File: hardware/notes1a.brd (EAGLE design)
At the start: 160 x 100 mm, 4 parts, among them U1 LMP7721, U2 MAX4477

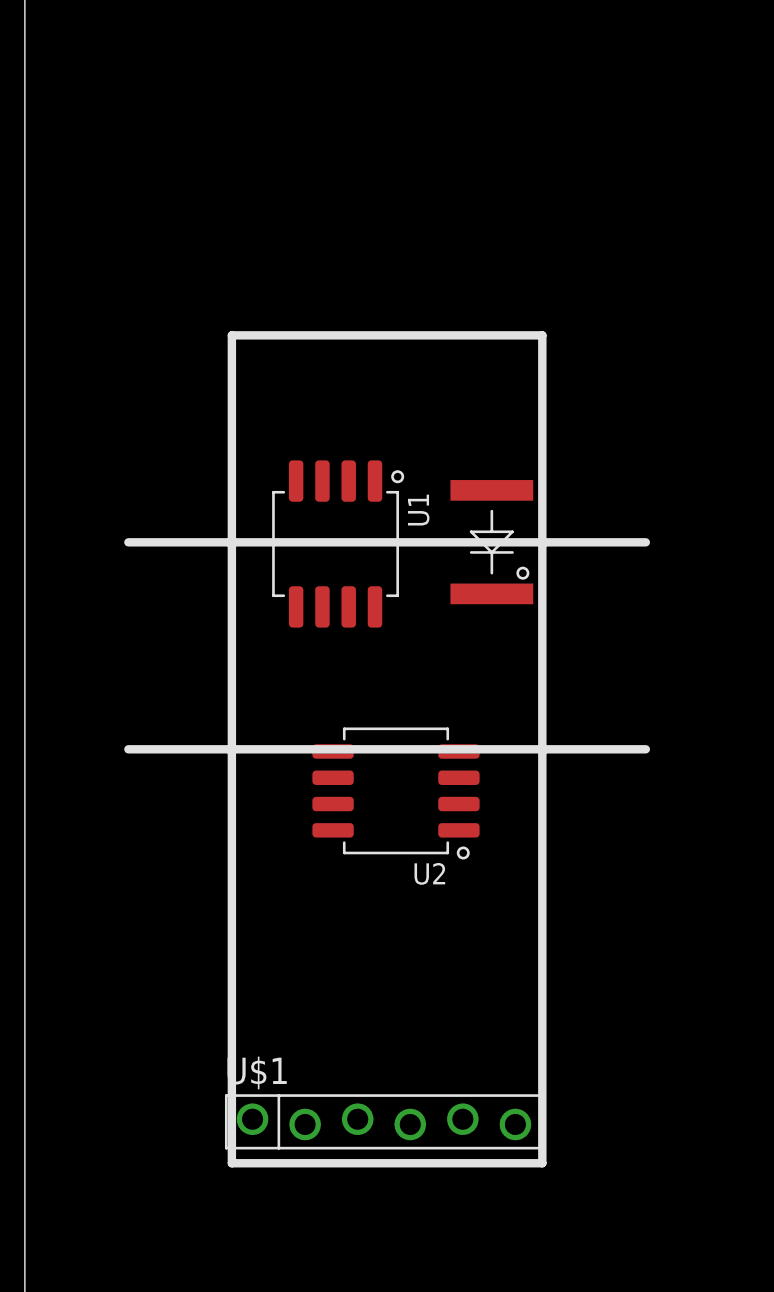
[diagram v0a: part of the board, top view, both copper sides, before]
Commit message: Added PIC microcontroller
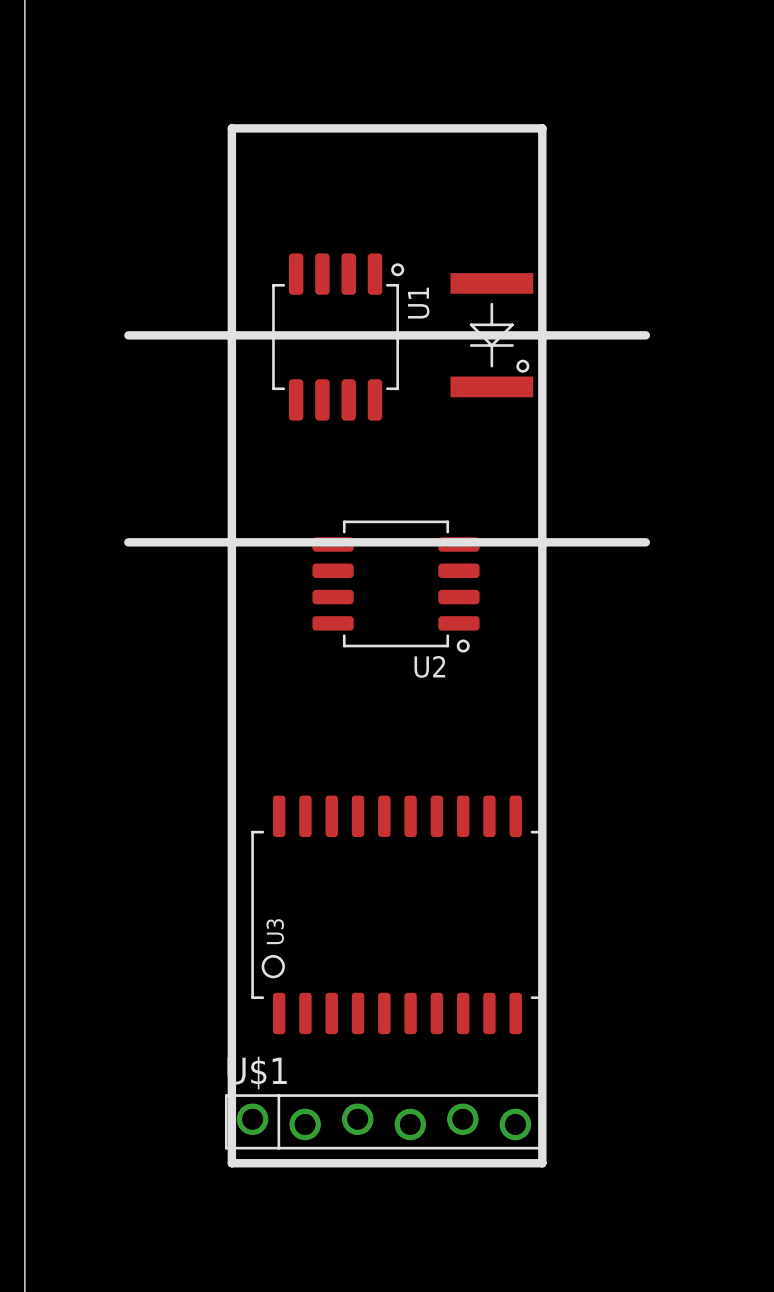
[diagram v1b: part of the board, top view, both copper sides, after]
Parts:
- added U3: PIC24FVXXKA301, openct:SOIC-20
- moved U2 10.0 mm to (17.9, 38.0)
- moved D1 10.0 mm to (23.1, 50.0)
- moved U1 10.0 mm to (15.0, 49.9)
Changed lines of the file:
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@@
 <wire x1="0" y1="100" x2="0" y2="0" width="0" layer="20"/>
 <wire x1="10" y1="10" x2="25" y2="10" width="0.4064" layer="21"/>
-<wire x1="25" y1="10" x2="25" y2="50" width="0.4064" layer="21"/>
-<wire x1="25" y1="50" x2="10" y2="50" width="0.4064" layer="21"/>
-<wire x1="10" y1="50" x2="10" y2="10" width="0.4064" layer="21"/>
-<wire x1="5" y1="30" x2="30" y2="30" width="0.4064" layer="21"/>
+<wire x1="25" y1="10" x2="25" y2="60" width="0.4064" layer="21"/>
+<wire x1="25" y1="60" x2="10" y2="60" width="0.4064" layer="21"/>
+<wire x1="10" y1="60" x2="10" y2="10" width="0.4064" layer="21"/>
 <wire x1="5" y1="40" x2="30" y2="40" width="0.4064" layer="21"/>
+<wire x1="5" y1="50" x2="30" y2="50" width="0.4064" layer="21"/>
 </plain>
 <attributes>
@@
 </autorouter>
 <elements>
-<element name="D1" library="openct" package="BPW34S-SIDEMOUNT" value="BPW34S" x="23.06" y="40.01" rot="R270"/>
-<element name="U1" library="openct" package="SOIC-8" value="LMP7721" x="15.01" y="39.92" rot="R180"/>
-<element name="U2" library="openct" package="SOIC-8" value="MAX4477" x="17.93" y="27.99" rot="R90"/>
+<element name="D1" library="openct" package="BPW34S-SIDEMOUNT" value="BPW34S" x="23.06" y="50.01" rot="R270"/>
+<element name="U1" library="openct" package="SOIC-8" value="LMP7721" x="15.01" y="49.92" rot="R180"/>
+<element name="U2" library="openct" package="SOIC-8" value="MAX4477" x="17.93" y="37.99" rot="R90"/>
 <element name="U$1" library="openct" package="1X06" value="1X06" x="11" y="12"/>
+<element name="U3" library="openct" package="SOIC-20" value="PIC24FVXXKA301" x="18" y="22"/>
 </elements>
 <signals>

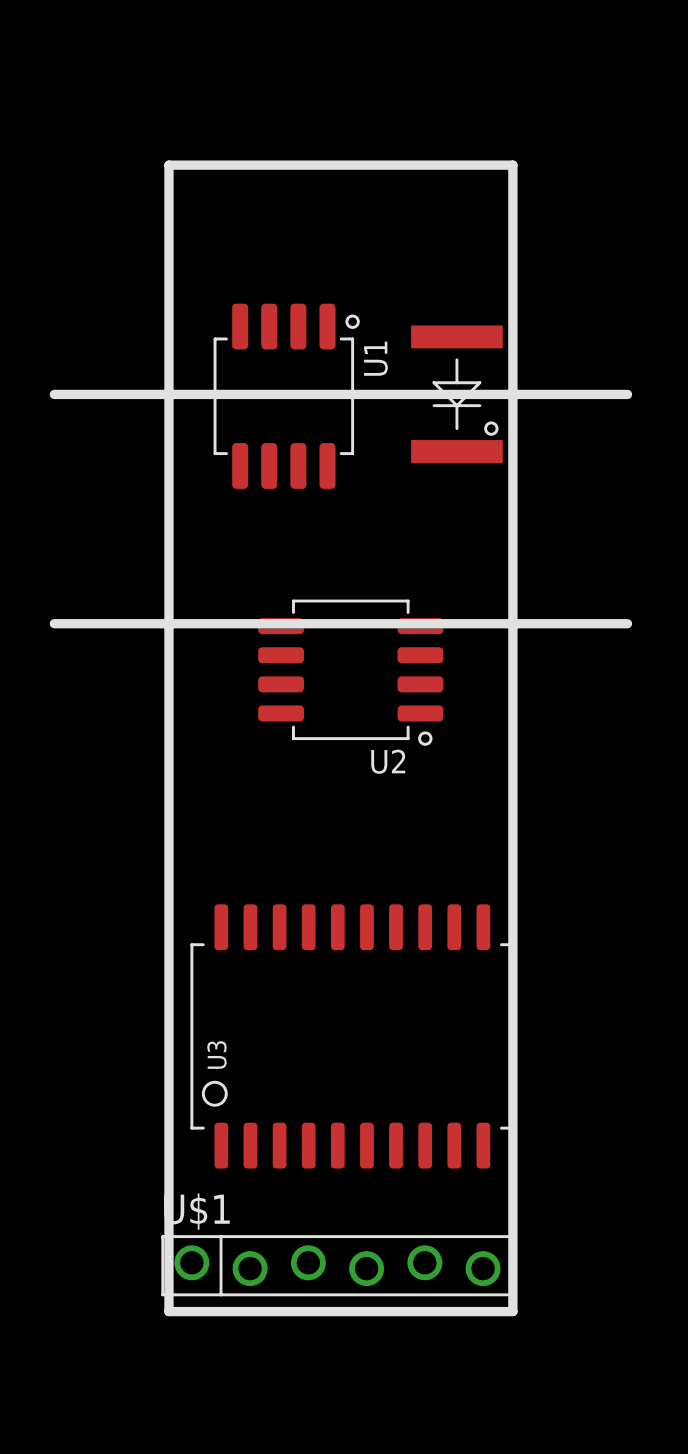
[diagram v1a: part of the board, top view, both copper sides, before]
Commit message: Added photodiode preamplifier
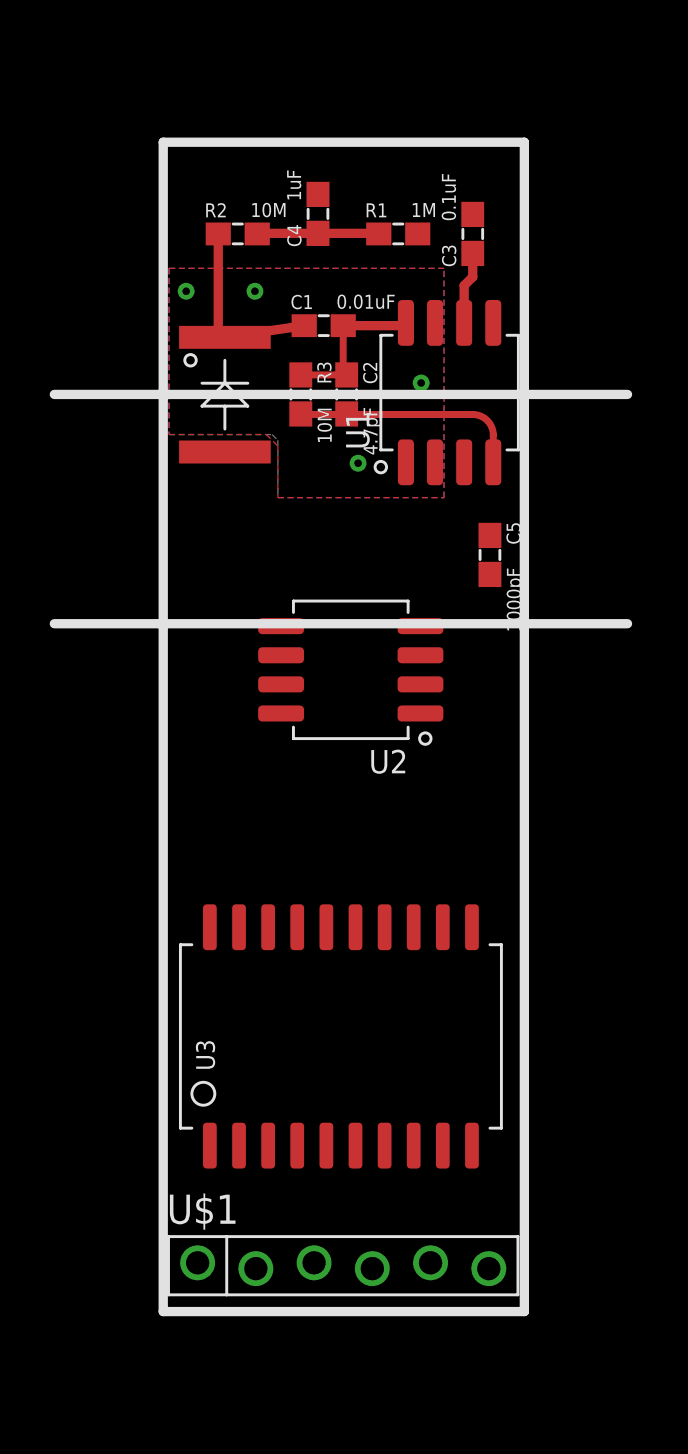
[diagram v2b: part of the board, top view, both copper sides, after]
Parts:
- added C1: 0.01uF, openct:0603
- added C2: 4.7pF, openct:0603
- added C3: 0.1uF, openct:0603
- added C4: 1uF, openct:0603
- added C5: 1000pF, openct:0603
- added R1: 1M, openct:0603
- added R2, R3: 10M, openct:0603
- moved D1 11.1 mm to (11.9, 50.0), turned to 90 degrees
- moved U1 7.23 mm to (22.2, 50.1), turned to 0 degrees
- moved U3 0.50 mm to (17.5, 22.0)
- moved U$1 0.25 mm to (11.2, 12.0)
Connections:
- new net 5V: C3.1, U1.6
- new net GND: C3.2, C4.2, D1.A, U1.3
- new net N$1: C1.2, C2.1, R3.1, U1.8
- new net N$10: C5.2
- new net N$2: C1.1, D1.C, R2.1
- new net N$4: C4.1, R1.1, R2.2
- new net N$7: C2.2, C5.1, R3.2, U1.4
- new net V/2: U1.1, U1.2, U1.7
- new net VBIAS: R1.2, U$1.6
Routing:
- net N$7: track 0.00 -> 9.99 mm
- net N$2: track 0.00 -> 8.30 mm
- net N$1: track 0.00 -> 7.00 mm
- net N$4: track 0.00 -> 5.34 mm
- net 5V: track 0.00 -> 3.19 mm
- added copper zone on layer 1, net V/2
- added copper zone on layer 16, net V/2
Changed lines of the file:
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@@
 <setting verticaltext="up"/>
 </settings>
-<grid distance="1" unitdist="mm" unit="mm" style="lines" multiple="1" display="yes" altdistance="0.025" altunitdist="inch" altunit="inch"/>
+<grid distance="0.25" unitdist="mm" unit="mm" style="lines" multiple="1" display="yes" altdistance="0.025" altunitdist="inch" altunit="inch"/>
 <layers>
 <layer number="1" name="Top" color="4" fill="1" visible="yes" active="yes"/>
@@
 <wire x1="160" y1="100" x2="0" y2="100" width="0" layer="20"/>
 <wire x1="0" y1="100" x2="0" y2="0" width="0" layer="20"/>
-<wire x1="10" y1="10" x2="25" y2="10" width="0.4064" layer="21"/>
-<wire x1="25" y1="10" x2="25" y2="60" width="0.4064" layer="21"/>
-<wire x1="25" y1="60" x2="10" y2="60" width="0.4064" layer="21"/>
-<wire x1="10" y1="60" x2="10" y2="10" width="0.4064" layer="21"/>
+<wire x1="9.75" y1="10" x2="25.5" y2="10" width="0.4064" layer="21"/>
+<wire x1="25.5" y1="10" x2="25.5" y2="61" width="0.4064" layer="21"/>
+<wire x1="25.5" y1="61" x2="9.75" y2="61" width="0.4064" layer="21"/>
+<wire x1="9.75" y1="61" x2="9.75" y2="10" width="0.4064" layer="21"/>
 <wire x1="5" y1="40" x2="30" y2="40" width="0.4064" layer="21"/>
 <wire x1="5" y1="50" x2="30" y2="50" width="0.4064" layer="21"/>
@@
 </autorouter>
 <elements>
-<element name="D1" library="openct" package="BPW34S-SIDEMOUNT" value="BPW34S" x="23.06" y="50.01" rot="R270"/>
-<element name="U1" library="openct" package="SOIC-8" value="LMP7721" x="15.01" y="49.92" rot="R180"/>
+<element name="D1" library="openct" package="BPW34S-SIDEMOUNT" value="BPW34S" x="11.94" y="49.99" rot="R90"/>
+<element name="U1" library="openct" package="SOIC-8" value="LMP7721" x="22.24" y="50.08"/>
 <element name="U2" library="openct" package="SOIC-8" value="MAX4477" x="17.93" y="37.99" rot="R90"/>
-<element name="U$1" library="openct" package="1X06" value="1X06" x="11" y="12"/>
-<element name="U3" library="openct" package="SOIC-20" value="PIC24FVXXKA301" x="18" y="22"/>
+<element name="U$1" library="openct" package="1X06" value="1X06" x="11.25" y="12"/>
+<element name="U3" library="openct" package="SOIC-20" value="PIC24FVXXKA301" x="17.5" y="22"/>
+<element name="C1" library="openct" package="0603" value="0.01uF" x="16.75" y="53"/>
+<element name="C2" library="openct" package="0603" value="4.7pF" x="17.75" y="50" rot="R270"/>
+<element name="C3" library="openct" package="0603" value="0.1uF" x="23.25" y="57" rot="R90"/>
+<element name="C4" library="openct" package="0603" value="1uF" x="16.5" y="57.875" rot="R90"/>
+<element name="R1" library="openct" package="0603" value="1M" x="20" y="57"/>
+<element name="R2" library="openct" package="0603" value="10M" x="13" y="57"/>
+<element name="R3" library="openct" package="0603" value="10M" x="15.75" y="50" rot="R270"/>
+<element name="C5" library="openct" package="0603" value="1000pF" x="24" y="43" rot="R270"/>
 </elements>
 <signals>
+<signal name="N$1">
+<contactref element="U1" pad="8"/>
+<contactref element="C1" pad="2"/>
+<contactref element="R3" pad="1"/>
+<contactref element="C2" pad="1"/>
+<wire x1="15.75" y1="50.85" x2="17.75" y2="50.85" width="0.3048" layer="1"/>
+<wire x1="17.6" y1="53" x2="17.6" y2="51" width="0.3048" layer="1"/>
+<wire x1="17.6" y1="51" x2="17.75" y2="50.85" width="0.3048" layer="1" curve="90"/>
+<wire x1="17.6" y1="53" x2="20.215" y2="53" width="0.4064" layer="1"/>
+<wire x1="20.215" y1="53" x2="20.335" y2="53.12" width="0.4064" layer="1" curve="90"/>
+</signal>
+<signal name="N$2">
+<contactref element="C1" pad="1"/>
+<contactref element="D1" pad="C"/>
+<contactref element="R2" pad="1"/>
+<wire x1="15.9" y1="53" x2="12.44" y2="52.49" width="0.4064" layer="1"/>
+<wire x1="12.15" y1="57" x2="12.15" y2="52.49" width="0.4064" layer="1"/>
+<wire x1="12.15" y1="52.49" x2="12.44" y2="52.49" width="0.4064" layer="1"/>
+</signal>
+<signal name="N$4">
+<contactref element="R2" pad="2"/>
+<contactref element="R1" pad="1"/>
+<contactref element="C4" pad="1"/>
+<wire x1="19.15" y1="57" x2="19.15" y2="57.025" width="0.4064" layer="1"/>
+<wire x1="19.15" y1="57.025" x2="16.5" y2="57.025" width="0.4064" layer="1"/>
+<wire x1="16.5" y1="57.025" x2="13.875" y2="57.025" width="0.4064" layer="1"/>
+<wire x1="13.875" y1="57.025" x2="13.85" y2="57" width="0.4064" layer="1" curve="90"/>
+</signal>
+<signal name="N$7">
+<contactref element="U1" pad="4"/>
+<contactref element="C5" pad="1"/>
+<contactref element="R3" pad="2"/>
+<contactref element="C2" pad="2"/>
+<wire x1="24.145" y1="47.04" x2="24.145" y2="48.23" width="0.3048" layer="1"/>
+<wire x1="24.145" y1="48.23" x2="23.25" y2="49.125" width="0.3048" layer="1" curve="90"/>
+<wire x1="23.25" y1="49.125" x2="17.75" y2="49.125" width="0.3048" layer="1"/>
+<wire x1="17.75" y1="49.125" x2="15.775" y2="49.125" width="0.3048" layer="1"/>
+<wire x1="15.775" y1="49.125" x2="15.75" y2="49.15" width="0.3048" layer="1" curve="-90"/>
+<wire x1="17.75" y1="49.15" x2="17.75" y2="49.125" width="0.3048" layer="1"/>
+<wire x1="24.145" y1="47.04" x2="24" y2="43.85" width="0" layer="19" extent="1-1"/>
+</signal>
+<signal name="GND">
+<contactref element="D1" pad="A"/>
+<contactref element="C4" pad="2"/>
+<contactref element="C3" pad="2"/>
+<contactref element="U1" pad="3"/>
+<wire x1="16.5" y1="58.725" x2="23.25" y2="57.85" width="0" layer="19" extent="1-1"/>
+<wire x1="22.875" y1="47.04" x2="23.25" y2="57.85" width="0" layer="19" extent="1-1"/>
+<wire x1="12.44" y1="47.49" x2="22.875" y2="47.04" width="0" layer="19" extent="1-1"/>
+</signal>
+<signal name="5V">
+<contactref element="U1" pad="6"/>
+<contactref element="C3" pad="1"/>
+<wire x1="22.875" y1="53.12" x2="22.875" y2="54.75" width="0.4064" layer="1"/>
+<wire x1="22.875" y1="54.75" x2="23.25" y2="55.125" width="0.4064" layer="1"/>
+<wire x1="23.25" y1="55.125" x2="23.25" y2="56.15" width="0.4064" layer="1"/>
+</signal>
+<signal name="N$10">
+<contactref element="C5" pad="2"/>
+</signal>
+<signal name="V/2">
+<contactref element="U1" pad="1"/>
+<contactref element="U1" pad="7"/>
+<contactref element="U1" pad="2"/>
+<polygon width="0.254" layer="1">
+<vertex x="22" y="45.5"/>
+<vertex x="22" y="55.5"/>
+<vertex x="10" y="55.5"/>
+<vertex x="10" y="48.25"/>
+<vertex x="14.25" y="48.25"/>
+<vertex x="14.75" y="47.75"/>
+<vertex x="14.75" y="45.5"/>
+</polygon>
+<polygon width="0.254" layer="16">
+<vertex x="22" y="45.5"/>
+<vertex x="22" y="55.5"/>
+<vertex x="10" y="55.5"/>
+<vertex x="10" y="48.25"/>
+<vertex x="14.5" y="48.25"/>
+<vertex x="14.75" y="48"/>
+<vertex x="14.75" y="45.5"/>
+</polygon>
+<via x="21" y="50.5" extent="1-16" drill="0.3302"/>
+<via x="18.25" y="47" extent="1-16" drill="0.3302"/>
+<via x="13.75" y="54.5" extent="1-16" drill="0.3302"/>
+<via x="10.75" y="54.5" extent="1-16" drill="0.3302"/>
+</signal>
+<signal name="VBIAS">
+<contactref element="R1" pad="2"/>
+<contactref element="U$1" pad="6"/>
+<wire x1="23.95" y1="11.873" x2="20.85" y2="57" width="0" layer="19" extent="1-1"/>
+</signal>
 </signals>
 </board>
